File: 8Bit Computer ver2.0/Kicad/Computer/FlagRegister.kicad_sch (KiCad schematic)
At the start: 9 parts, among them IC125 SN74LVC1G14DBVR, IC126 SN74AHC32DR, IC127 SN74HCS4075DR, IC128 SN74AHC08DR, IC129 SN74AHC74DR, IC130 SN74AHC74DR, IC131 SN74AHC74DR, IC132 SN74AHC08DR, IC133 SN74ABT574ADWR

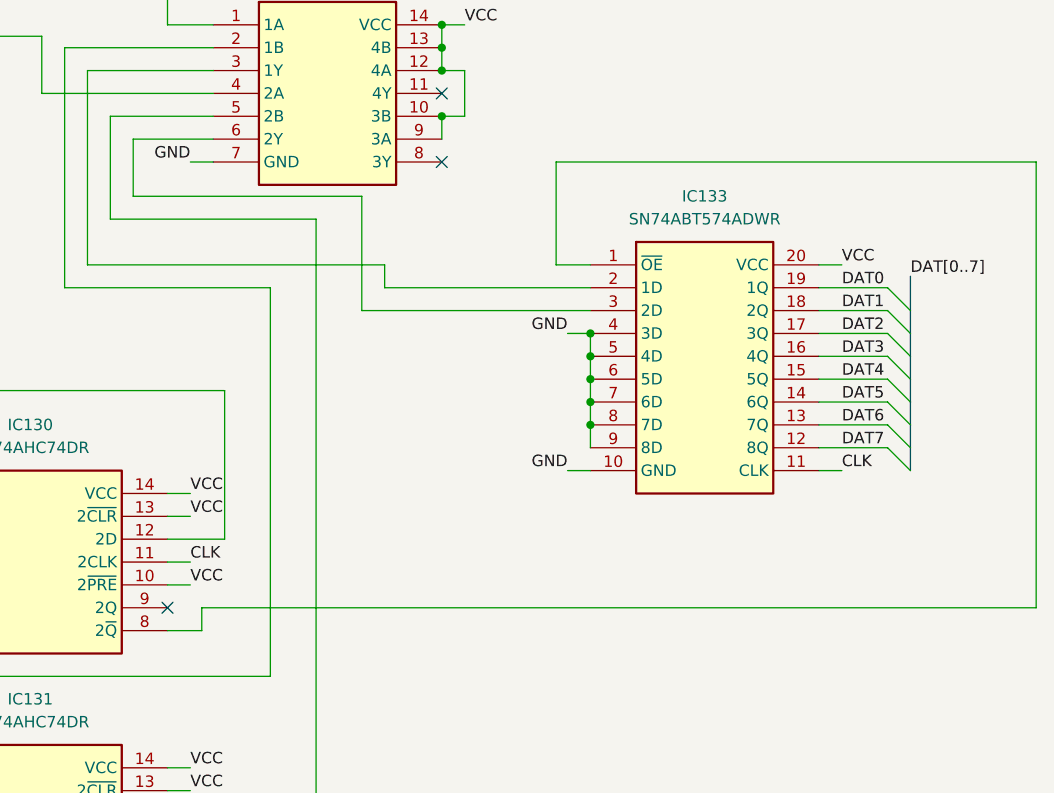
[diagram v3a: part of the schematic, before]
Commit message: Kicad
fixed some design errors(dat dis DistShiftreg, wrong cmd pins)
added description to every CMD for better debug, use CTRL+f and use option "Whole words only" to search e.g. inc
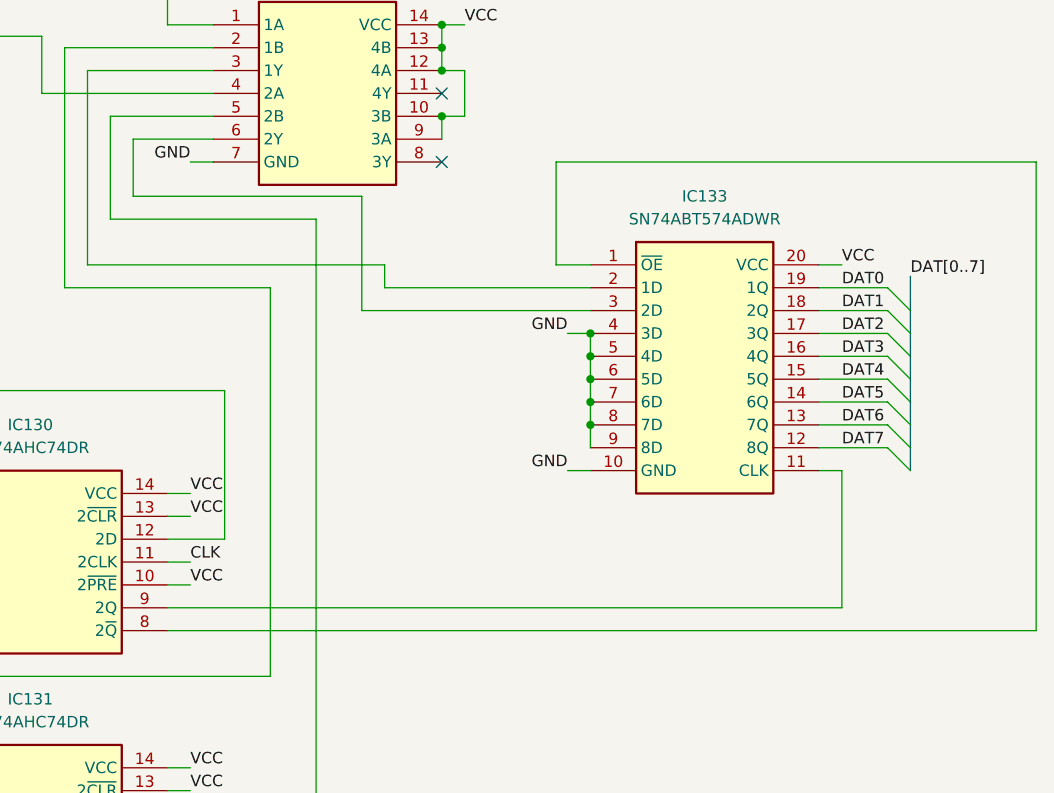
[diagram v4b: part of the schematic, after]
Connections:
- net CLK: no longer IC133.11 (CLK)
- net at IC130.9 (2Q): now also IC133.11 (CLK)
- no-connect marks 11 -> 10
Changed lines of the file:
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@@
-	)
-	(no_connect
-		(at 182.88 111.76)
 	)
 	(no_connect
@@
 	(wire
 		(pts
-			(xy 279.4 111.76) (xy 279.4 62.23)
+			(xy 279.4 114.3) (xy 279.4 62.23)
 		)
 		(stroke
@@
 	(wire
 		(pts
-			(xy 182.88 114.3) (xy 186.69 114.3)
+			(xy 182.88 114.3) (xy 279.4 114.3)
 		)
 		(stroke
@@
 	(wire
 		(pts
-			(xy 186.69 111.76) (xy 186.69 114.3)
-		)
-		(stroke
-			(width 0)
-			(type default)
-		)
-	)
-	(wire
-		(pts
 			(xy 182.88 25.4) (xy 182.88 46.99)
 		)
@@
 	(wire
 		(pts
+			(xy 257.81 96.52) (xy 257.81 111.76)
+		)
+		(stroke
+			(width 0)
+			(type default)
+		)
+	)
+	(wire
+		(pts
 			(xy 171.45 76.2) (xy 171.45 49.53)
 		)
@@
 	(wire
 		(pts
+			(xy 182.88 111.76) (xy 257.81 111.76)
+		)
+		(stroke
+			(width 0)
+			(type default)
+		)
+	)
+	(wire
+		(pts
 			(xy 255.27 78.74) (xy 262.89 78.74)
 		)
@@
 			(type default)
 			(color 121 255 176 1)
-		)
-	)
-	(wire
-		(pts
-			(xy 186.69 111.76) (xy 279.4 111.76)
-		)
-		(stroke
-			(width 0)
-			(type default)
 		)
 	)
@@
 		)
 	)
-	(label "CLK"
-		(at 257.81 96.52 0)
-		(effects
-			(font
-				(size 1.27 1.27)
-			)
-			(justify left bottom)
-		)
-	)

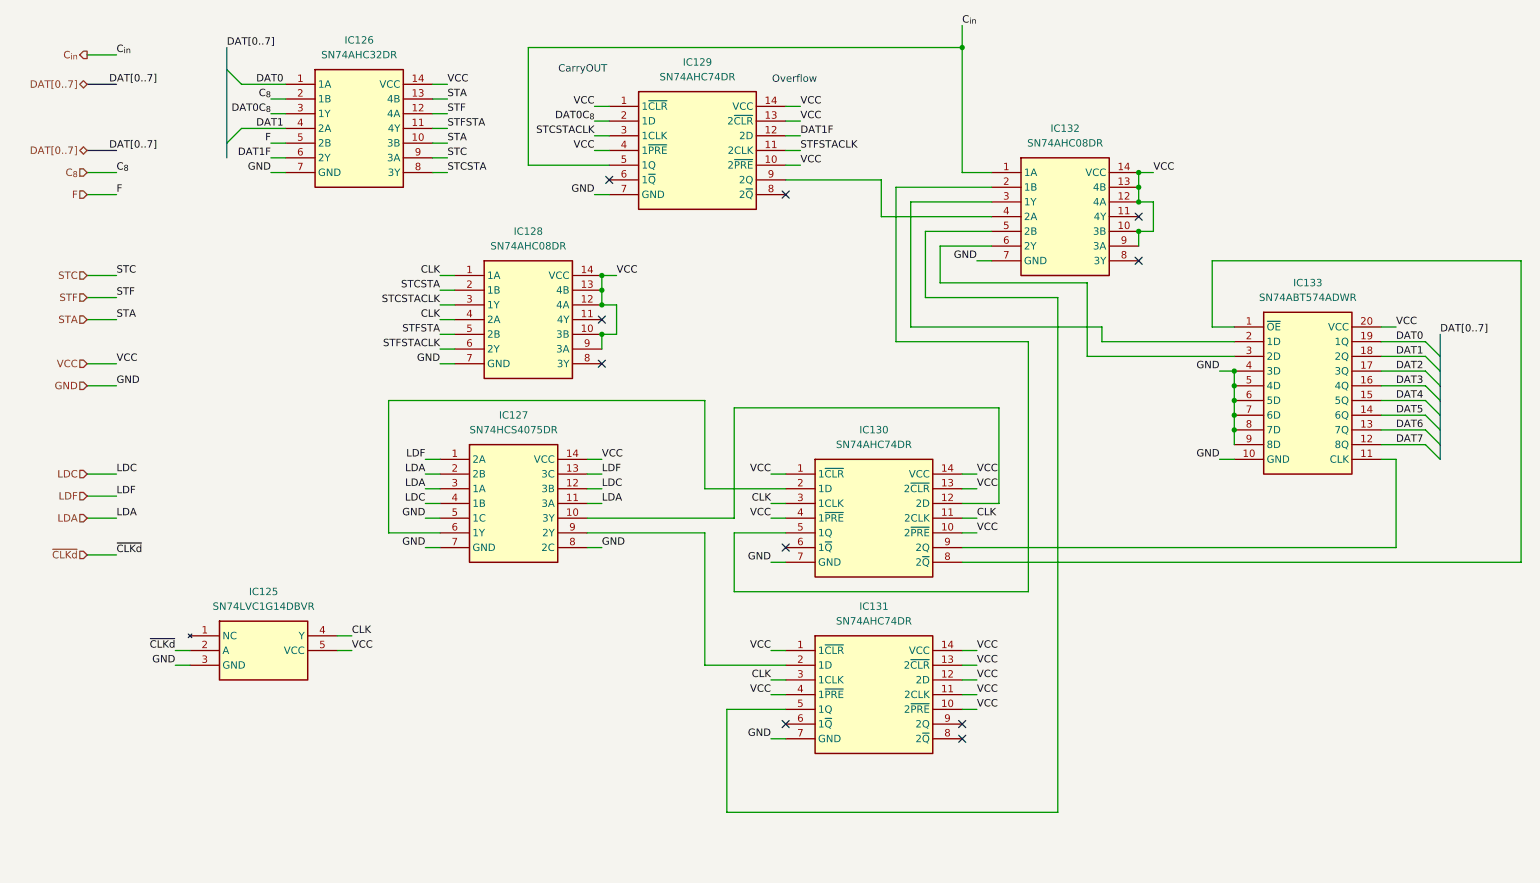
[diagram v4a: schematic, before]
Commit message: changed page numbers, compressed ROOT file from A1 to A4
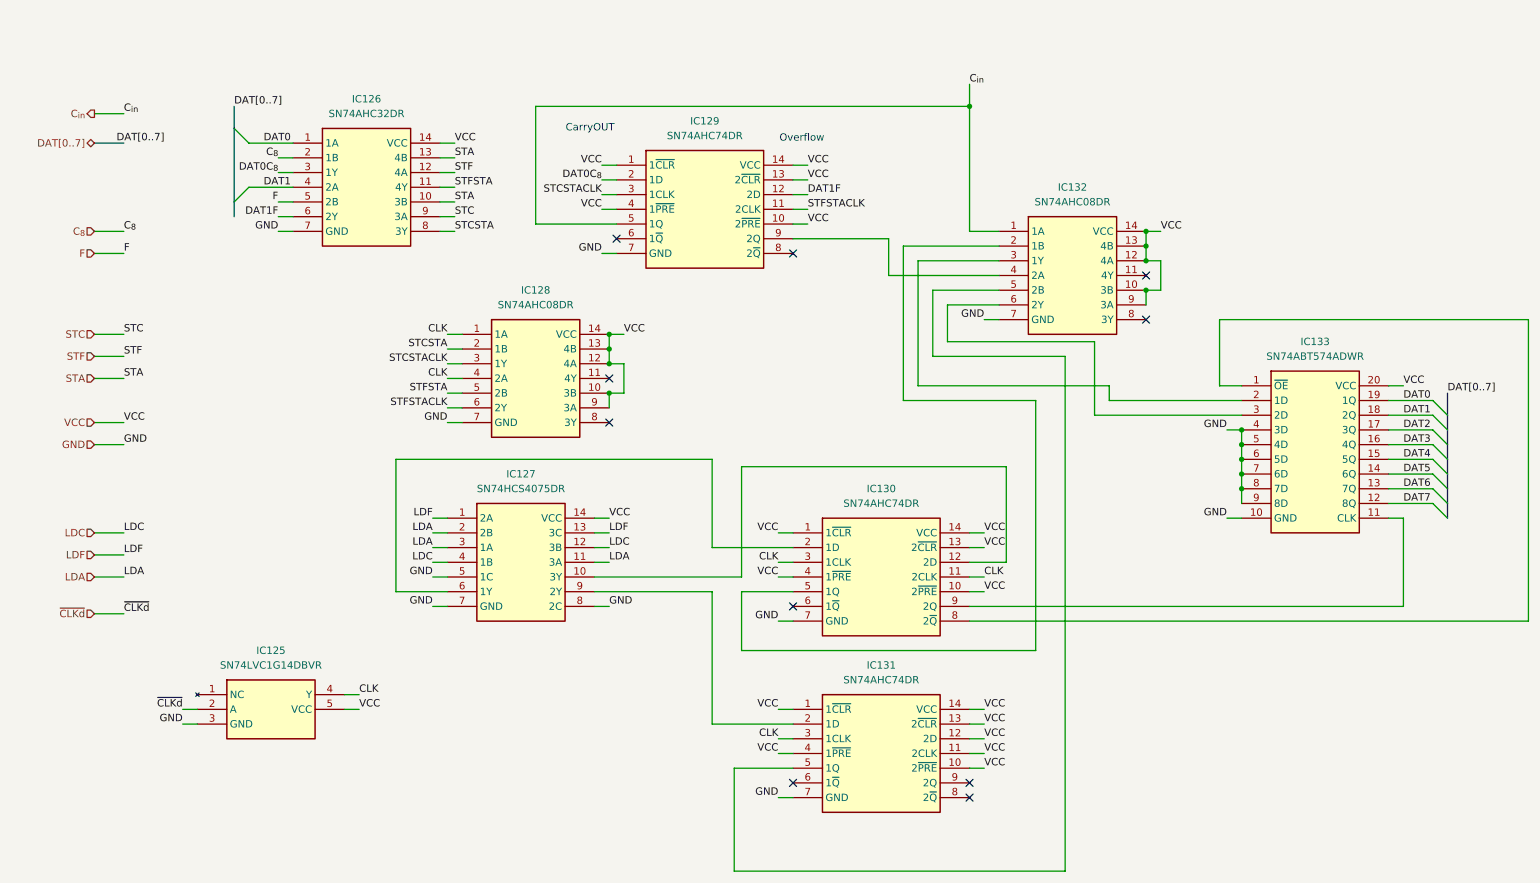
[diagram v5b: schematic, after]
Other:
- moved on the sheet: IC125, IC126, IC127, IC128, IC129, IC130, IC131, IC132, IC133

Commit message: changed page numbers, every schematic is now A4
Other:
- title: (none) -> ${SHEETNAME}
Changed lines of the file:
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@@
 	(generator_version "9.0")
 	(paper "A4")
+	(title_block
+		(title "${SHEETNAME}")
+		(date "2026-03-21")
+		(rev "2.7")
+	)
 	(text "Overflow"
 		(exclude_from_sim no)
